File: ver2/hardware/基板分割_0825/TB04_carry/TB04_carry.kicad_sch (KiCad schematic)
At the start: 1 part, among them J1 Conn_02x10_Odd_Even

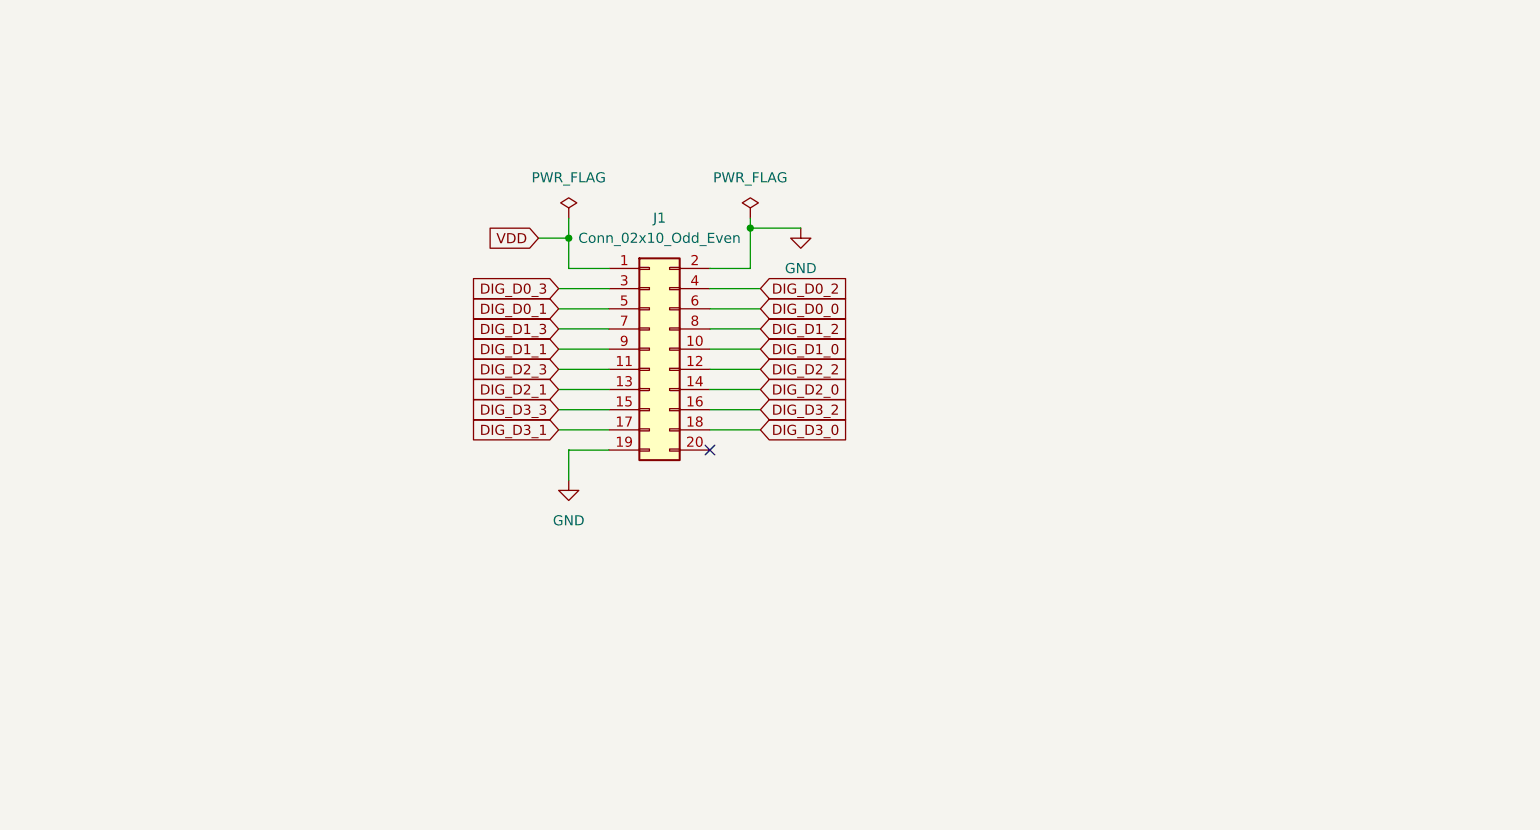
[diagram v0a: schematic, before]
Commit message: ver2: キャリアに7segIF用2×5コネクタ4個と電源部を実装／全7枚に予備の端子台
- キャリア: J3-J6(2×5)が桁1-4で表と全一致・DIG_*16ネットは2ピン構成
  (isolated_pin_label 16件→0件)、C1/C2/電源LED/端子台を追加
- 入力の2×10はJ1→J2にリナンバー(20ピンの中身は表と一致)
- 7枚とも端子台J1602を1個ずつ追加(pin1=＋/pin2=GNDで向きは全枚統一)
- 署名比較で既存ピンのネット変化は7枚とも0件(吸着なし)

Co-Authored-By: Claude Opus 5 <noreply@anthropic.com>
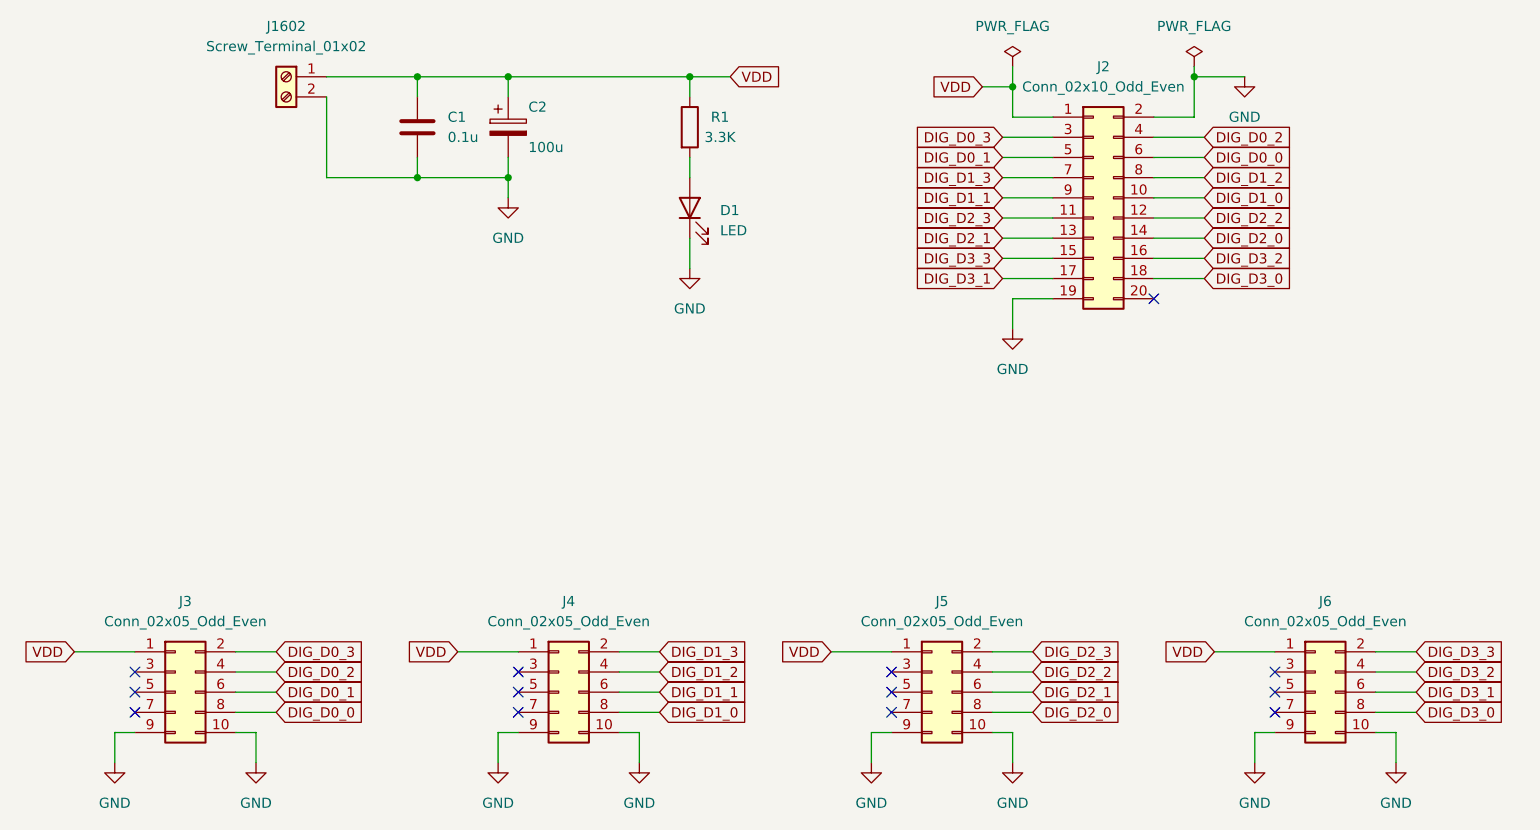
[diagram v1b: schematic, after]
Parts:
- added C1: 0.1u, Capacitor_THT:C_Disc_D4.3mm_W1.9mm_P5.00mm, symbol Device:C
- added C2: 100u, Capacitor_THT:CP_Radial_D5.0mm_P2.00mm, symbol Device:C_Polarized
- added D1: LED, LED_THT:LED_D3.0mm_Clear, symbol Device:LED
- added J1602: Screw_Terminal_01x02, symbol Connector:Screw_Terminal_01x02
- added J3, J4, J5, J6: Conn_02x05_Odd_Even, Connector_PinSocket_2.54mm:PinSocket_2x05_P2.54mm_Vertical, symbol Connector_Generic:Conn_02x05_Odd_Even
- added R1: 3.3K, Resistor_THT:R_Axial_DIN0207_L6.3mm_D2.5mm_P7.62mm_Horizontal, symbol Device:R
- renumbered J1 to J2
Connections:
- net DIG_D0_0: now also J3.8 (Pin_8)
- net DIG_D0_1: now also J3.6 (Pin_6)
- net DIG_D0_2: now also J3.4 (Pin_4)
- net DIG_D0_3: now also J3.2 (Pin_2)
- net DIG_D1_0: now also J4.8 (Pin_8)
- net DIG_D1_1: now also J4.6 (Pin_6)
- net DIG_D1_2: now also J4.4 (Pin_4)
- net DIG_D1_3: now also J4.2 (Pin_2)
- net DIG_D2_0: now also J5.8 (Pin_8)
- net DIG_D2_1: now also J5.6 (Pin_6)
- net DIG_D2_2: now also J5.4 (Pin_4)
- net DIG_D2_3: now also J5.2 (Pin_2)
- net DIG_D3_0: now also J6.8 (Pin_8)
- net DIG_D3_1: now also J6.6 (Pin_6)
- net DIG_D3_2: now also J6.4 (Pin_4)
- net DIG_D3_3: now also J6.2 (Pin_2)
- net GND: now also C1.2, C2.2, D1.1 (K), J1602.2 (Pin_2), J3.10 (Pin_10), J3.9 (Pin_9), J4.10 (Pin_10), J4.9 (Pin_9), J5.10 (Pin_10), J5.9 (Pin_9), J6.10 (Pin_10), J6.9 (Pin_9)
- net VDD: now also C1.1, C2.1, J1602.1 (Pin_1), J3.1 (Pin_1), J4.1 (Pin_1), J5.1 (Pin_1), J6.1 (Pin_1), R1.1
- new net: D1.2 (A), R1.2
- no-connect marks 1 -> 13
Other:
- moved on the sheet: J2

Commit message: ver2: キャリア基板TB04_carryのPCBレイアウトを取り込み
ver1のTB04addr4bitVer3.kicad_proはKiCADによる自動更新(電気的変更なし)。

Co-Authored-By: Claude Opus 5 <noreply@anthropic.com>
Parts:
- J1602: footprint (none) -> TerminalBlock:TerminalBlock_MaiXu_MX126-5.0-02P_1x02_P5.00mm
- J2: footprint (none) -> Connector_PinSocket_2.54mm:PinSocket_2x10_P2.54mm_Vertical
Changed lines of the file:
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@@
 			)
 		)
-		(property "Footprint" ""
+		(property "Footprint" "Connector_PinSocket_2.54mm:PinSocket_2x10_P2.54mm_Vertical"
 			(at 168.91 62.23 0)
 			(hide yes)
@@
 			)
 		)
-		(property "Footprint" ""
+		(property "Footprint" "TerminalBlock:TerminalBlock_MaiXu_MX126-5.0-02P_1x02_P5.00mm"
 			(at 67.31 46.99 0)
 			(hide yes)
